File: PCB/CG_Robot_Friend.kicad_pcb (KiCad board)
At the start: 2 copper layers, 62.2 x 85.7 mm, 26 parts, among them J1 PROTO, J10 PROTO, J11 PROTO, J12 PROTO, J2 PROTO, J3 PROTO, J4 PROTO, J5 PROTO, J6 PROTO, J7 PROTO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

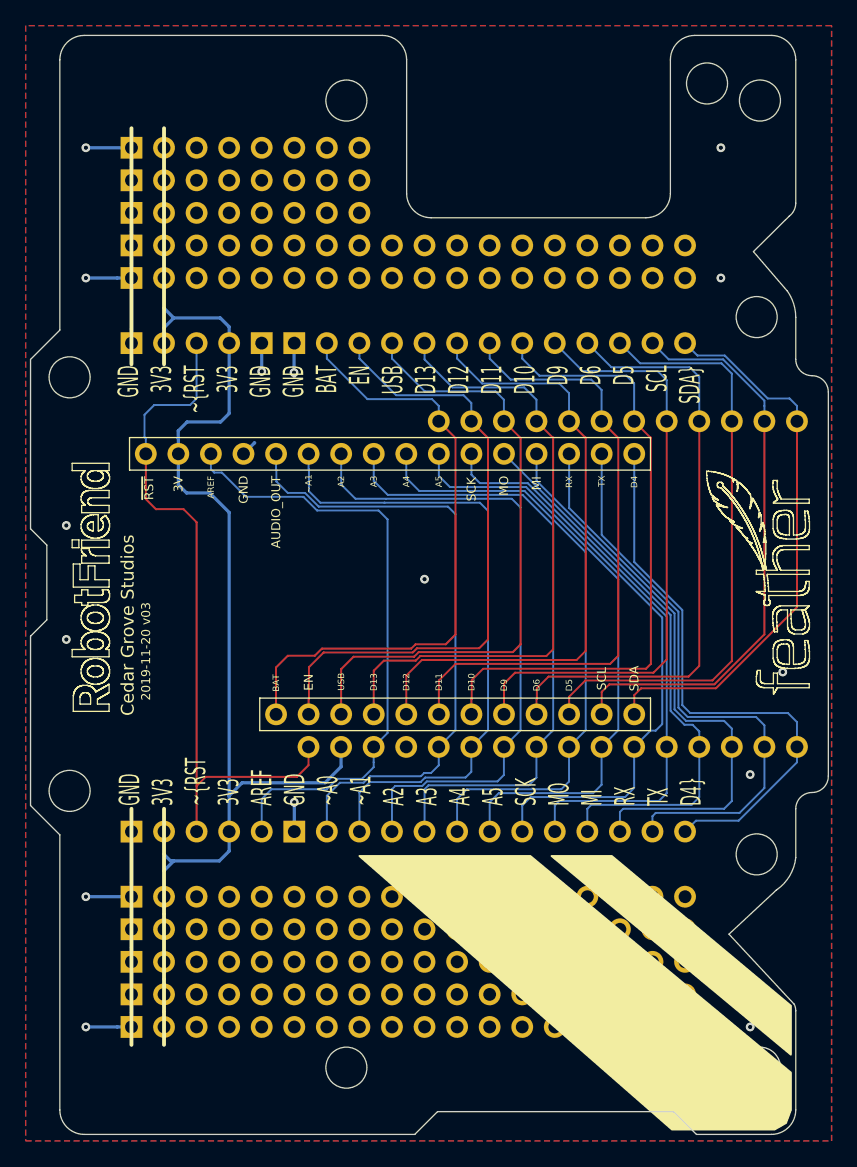
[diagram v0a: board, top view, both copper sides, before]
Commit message: update to PCB v04: enhance cutout
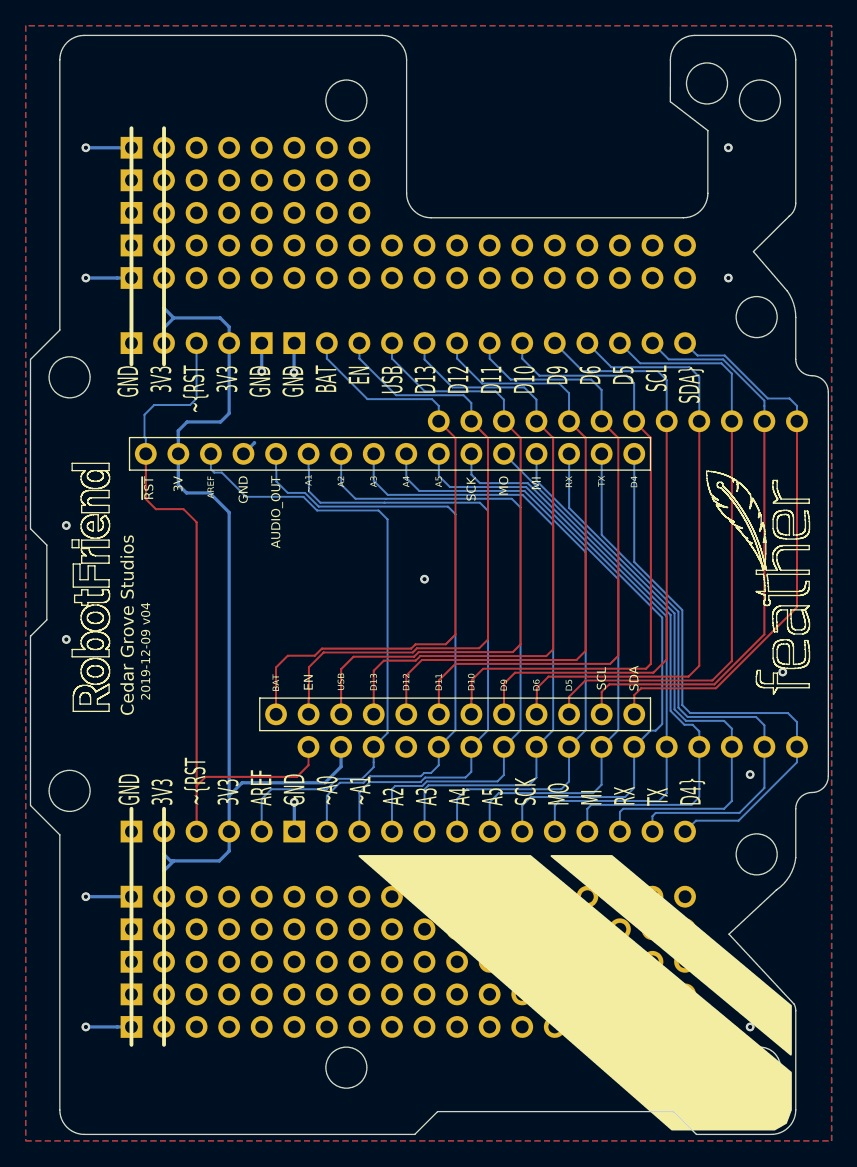
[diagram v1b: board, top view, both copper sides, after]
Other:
- outline, holes or cut-outs redrawn
- board text added: "2019-12-09 v04"
- board text removed: "2019-11-20 v03"
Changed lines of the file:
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@@
   (general
     (thickness 1.6)
-    (drawings 29082)
+    (drawings 29084)
     (tracks 424)
     (zones 0)
@@
   (title_block
     (title Robot_Friend_FeatherWing)
-    (date 2019-11-20)
-    (rev v03)
+    (date 2019-12-09)
+    (rev v04)
     (company "Cedar Grove Studios")
   )
@@
       (net 3 /SDA))
     (model "C:/Program Files/KiCad/share/kicad/packages3d/Adafruit_CAD_Parts-master/3093 Crickit CPX/3093 Crickit CPX.step"
-      (offset (xyz 1 0 -44))
+      (offset (xyz 1 0 -11))
       (scale (xyz 1 1 1))
       (rotate (xyz 0 0 90))
@@
     )
   )
+  (gr_line (start 136.4 52) (end 133.475 49.75) (layer Edge.Cuts) (width 0.1))
+  (gr_line (start 136.4 52) (end 136.4 56.9) (layer Edge.Cuts) (width 0.1))
   (gr_poly (pts (xy 124.206 108.585) (xy 128.905 108.585) (xy 142.875 120.269) (xy 142.875 124.079)) (layer F.SilkS) (width 0.15))
   (gr_line (start 139.954 61.4426) (end 142.748 58.674) (layer Edge.Cuts) (width 0.1))
@@
   (gr_line (start 133.477 46.609) (end 141.605 46.609) (layer B.SilkS) (width 1))
   (gr_line (start 135.382 44.577) (end 141.351 44.577) (layer Edge.Cuts) (width 0.1))
-  (gr_line (start 114.808 58.801) (end 131.572 58.801) (layer Edge.Cuts) (width 0.1))
-  (gr_line (start 133.477 46.482) (end 133.477 56.896) (layer Edge.Cuts) (width 0.1))
+  (gr_line (start 114.808 58.801) (end 134.5 58.8) (layer Edge.Cuts) (width 0.1))
+  (gr_line (start 133.477 46.482) (end 133.475 49.75) (layer Edge.Cuts) (width 0.1))
   (gr_line (start 112.903 46.482) (end 112.903 56.896) (layer Edge.Cuts) (width 0.1))
-  (gr_arc (start 131.572 56.896) (end 131.572 58.801) (angle -90) (layer Edge.Cuts) (width 0.1))
+  (gr_arc (start 134.495 56.896) (end 134.495 58.801) (angle -90) (layer Edge.Cuts) (width 0.1))
   (gr_arc (start 114.808 56.896) (end 112.903 56.896) (angle -90) (layer Edge.Cuts) (width 0.1))
   (gr_arc (start 135.382 46.482) (end 135.382 44.577) (angle -90) (layer Edge.Cuts) (width 0.1))
@@
   (gr_line (start 89.501722 78.610179) (end 89.523722 78.610179) (layer F.SilkS) (width 0.1))
   (gr_line (start 89.501722 78.589079) (end 89.501722 78.610179) (layer F.SilkS) (width 0.1))
-  (gr_text "2019-11-20 v03" (at 92.62 92.84 90) (layer B.SilkS)
+  (gr_text "2019-12-09 v04" (at 92.62 92.84 90) (layer B.SilkS)
     (effects (font (size 0.7 0.7) (thickness 0.1)) (justify mirror))
   )
@@
   (gr_arc (start 144.526 69.85) (end 143.256 69.85) (angle -90) (layer Edge.Cuts) (width 0.1))
   (gr_arc (start 144.526 72.39) (end 145.796 72.39) (angle -90) (layer Edge.Cuts) (width 0.1))
-  (gr_text "2019-11-20 v03" (at 92.57 92.62 90) (layer F.SilkS)
+  (gr_text "2019-12-09 v04" (at 92.57 92.62 90) (layer F.SilkS)
     (effects (font (size 0.7 0.7) (thickness 0.1)))
   )
@@
   (via (at 86.36 91.694) (size 0.6858) (drill 0.3302) (layers F.Cu B.Cu) (net 1))
   (via (at 86.36 82.804) (size 0.6858) (drill 0.3302) (layers F.Cu B.Cu) (net 1))
-  (via (at 137.414 63.5) (size 0.6858) (drill 0.3302) (layers F.Cu B.Cu) (net 1))
+  (via (at 138 63.5) (size 0.6858) (drill 0.3302) (layers F.Cu B.Cu) (net 1))
   (via (at 87.884 63.5) (size 0.6858) (drill 0.3302) (layers F.Cu B.Cu) (net 1))
-  (via (at 137.414 53.34) (size 0.6858) (drill 0.3302) (layers F.Cu B.Cu) (net 1))
+  (via (at 138 53.34) (size 0.6858) (drill 0.3302) (layers F.Cu B.Cu) (net 1))
   (via (at 87.884 53.34) (size 0.6858) (drill 0.3302) (layers F.Cu B.Cu) (net 1))
   (via (at 139.7 121.92) (size 0.6858) (drill 0.3302) (layers F.Cu B.Cu) (net 1))
